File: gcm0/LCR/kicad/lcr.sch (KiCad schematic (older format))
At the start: 89 parts, among them J1 Conn_01x02_Male, J2 Conn_01x02_Male, J3 Conn_01x03_Male, Q1 BC547, Q2 BC547, SW1 SW_Push, SW2 SW_Push, U1 MCP6022, U10 LM1117-3.3, U11 CD4052BCN, U2 HCF4053BE, U3 CD4052BCN, U4 LM317_TO-220, U5 MCP6022, U6 MCP6022, U7 LM358, U8 STM32F030F4P6, U9 74HC595, Y1 8MHZ

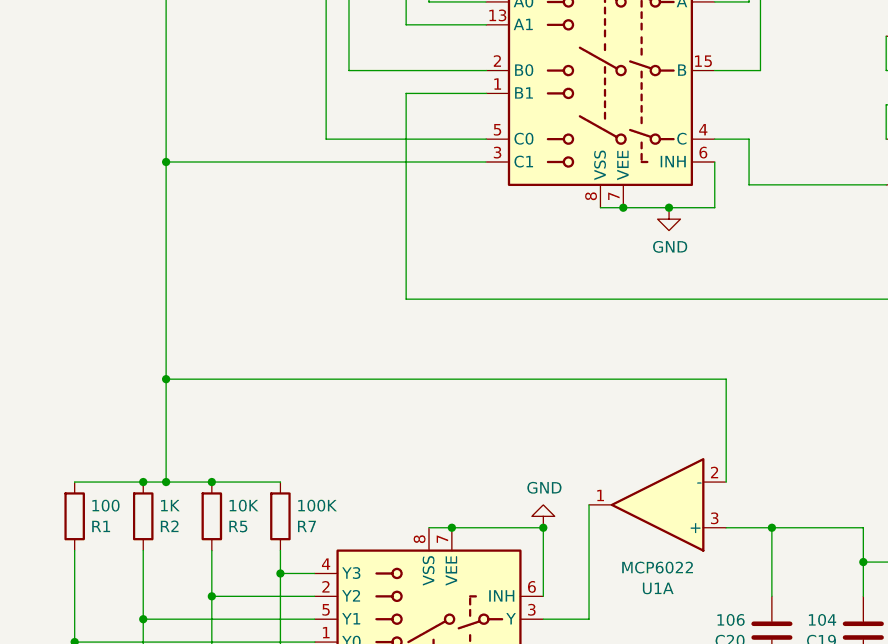
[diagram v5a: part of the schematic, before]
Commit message: 电路少画一个电阻
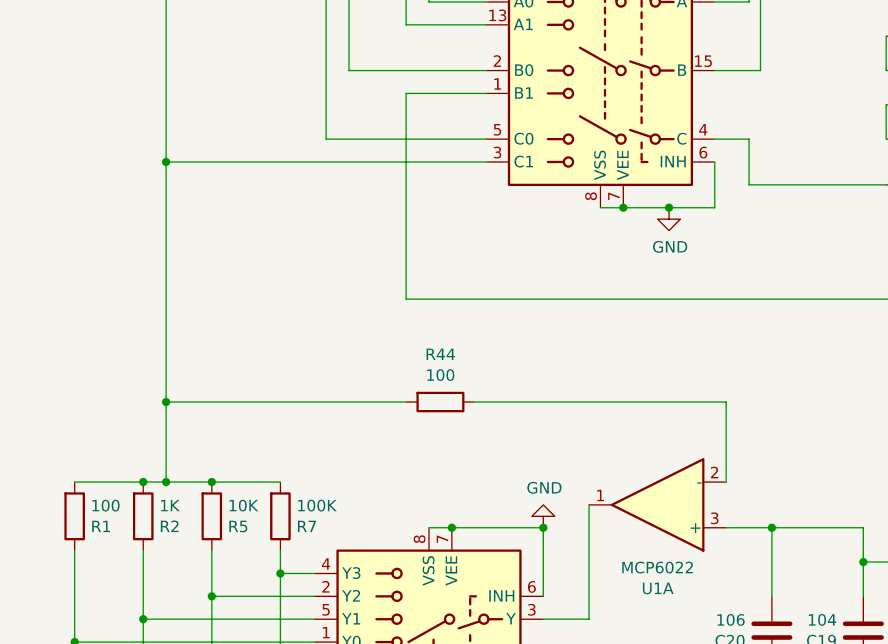
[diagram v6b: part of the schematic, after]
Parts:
- added R44: 100, symbol Device:R
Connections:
- net at J2.2 (Pin_2), R1.2, R2.2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: now also R44.2; no longer U1.2 (-)
- new net: R44.1, U1.2 (-)
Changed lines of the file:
@@
 	1800 5950 2000 5950
-Wire Wire Line
-	4250 5950 4250 5500
-Wire Wire Line
-	4250 5500 1800 5500
-Connection ~ 1800 5500
-Wire Wire Line
-	1800 5500 1800 5950
 Wire Wire Line
 	3450 7050 5700 7050
@@
 	3200 4550 1800 4550
 Connection ~ 1800 4550
-Wire Wire Line
-	1800 4550 1800 5500
 Wire Wire Line
 	14250 5850 14550 5850
@@
 	1    0    0    -1
 $EndComp
+Wire Wire Line
+	1800 4550 1800 5600
+$Comp
+L Device:R R44
+U 1 1 61282B84
+P 3000 5600
+F 0 "R44" V 2793 5600 50  0000 C CNN
+F 1 "100" V 2884 5600 50  0000 C CNN
+F 2 "" V 2930 5600 50  0001 C CNN
+F 3 "~" H 3000 5600 50  0001 C CNN
+	1    3000 5600
+	0    1    1    0
+$EndComp
+Wire Wire Line
+	3150 5600 4250 5600
+Wire Wire Line
+	4250 5600 4250 5950
+Wire Wire Line
+	2850 5600 1800 5600
+Connection ~ 1800 5600
+Wire Wire Line
+	1800 5600 1800 5950
 $EndSCHEMATC
